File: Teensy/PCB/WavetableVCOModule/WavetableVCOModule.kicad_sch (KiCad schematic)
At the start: 11 parts, among them J1 Micro_SD_Card, SW1 Next_File_Button, U1 SPI_Oled, U2 Teensy4.0

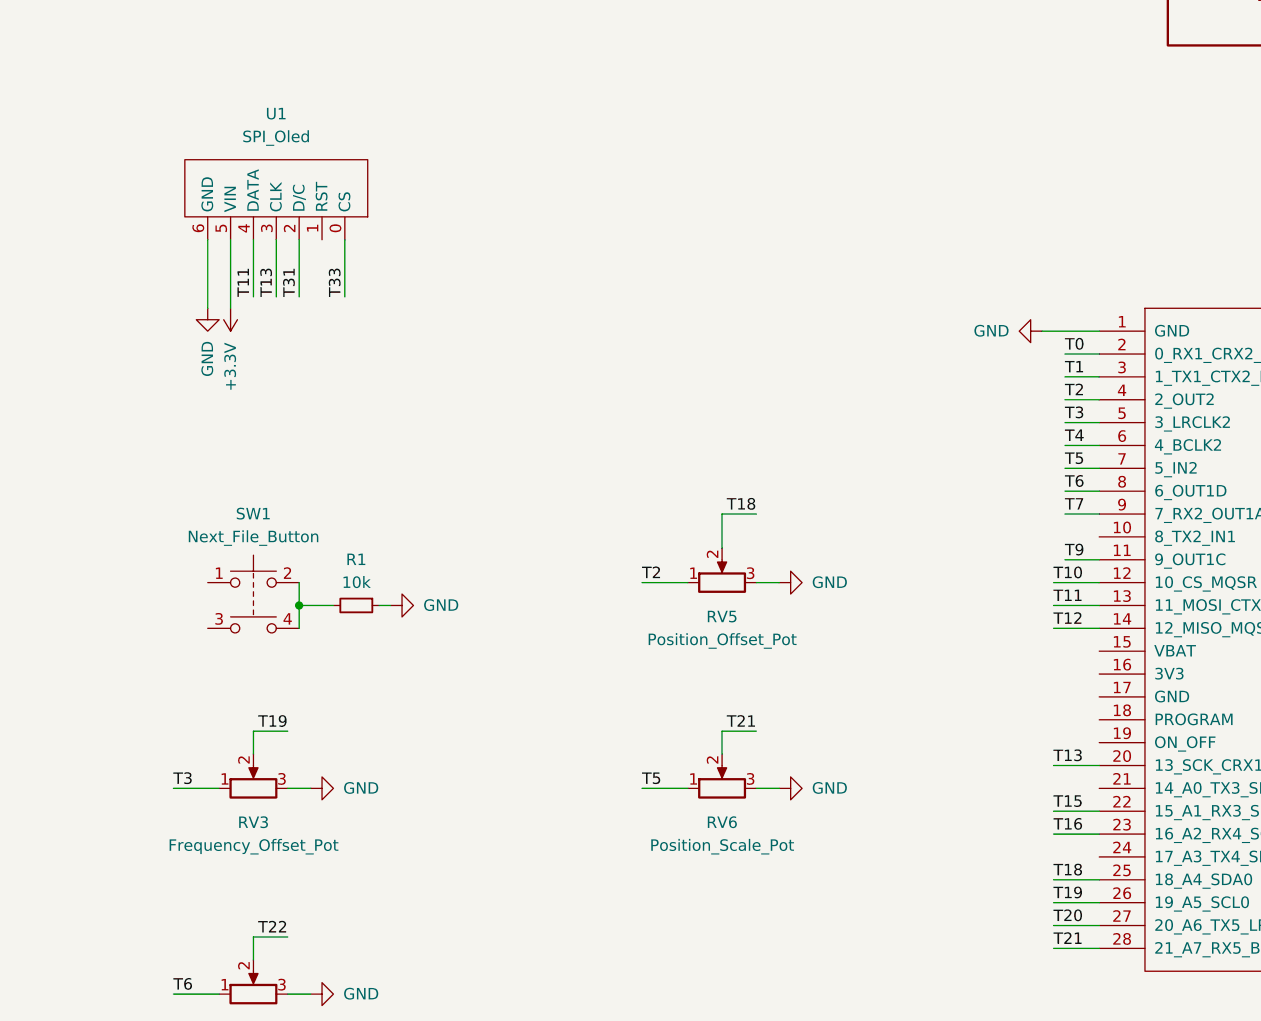
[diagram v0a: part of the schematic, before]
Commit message: Added Wavetable VCO
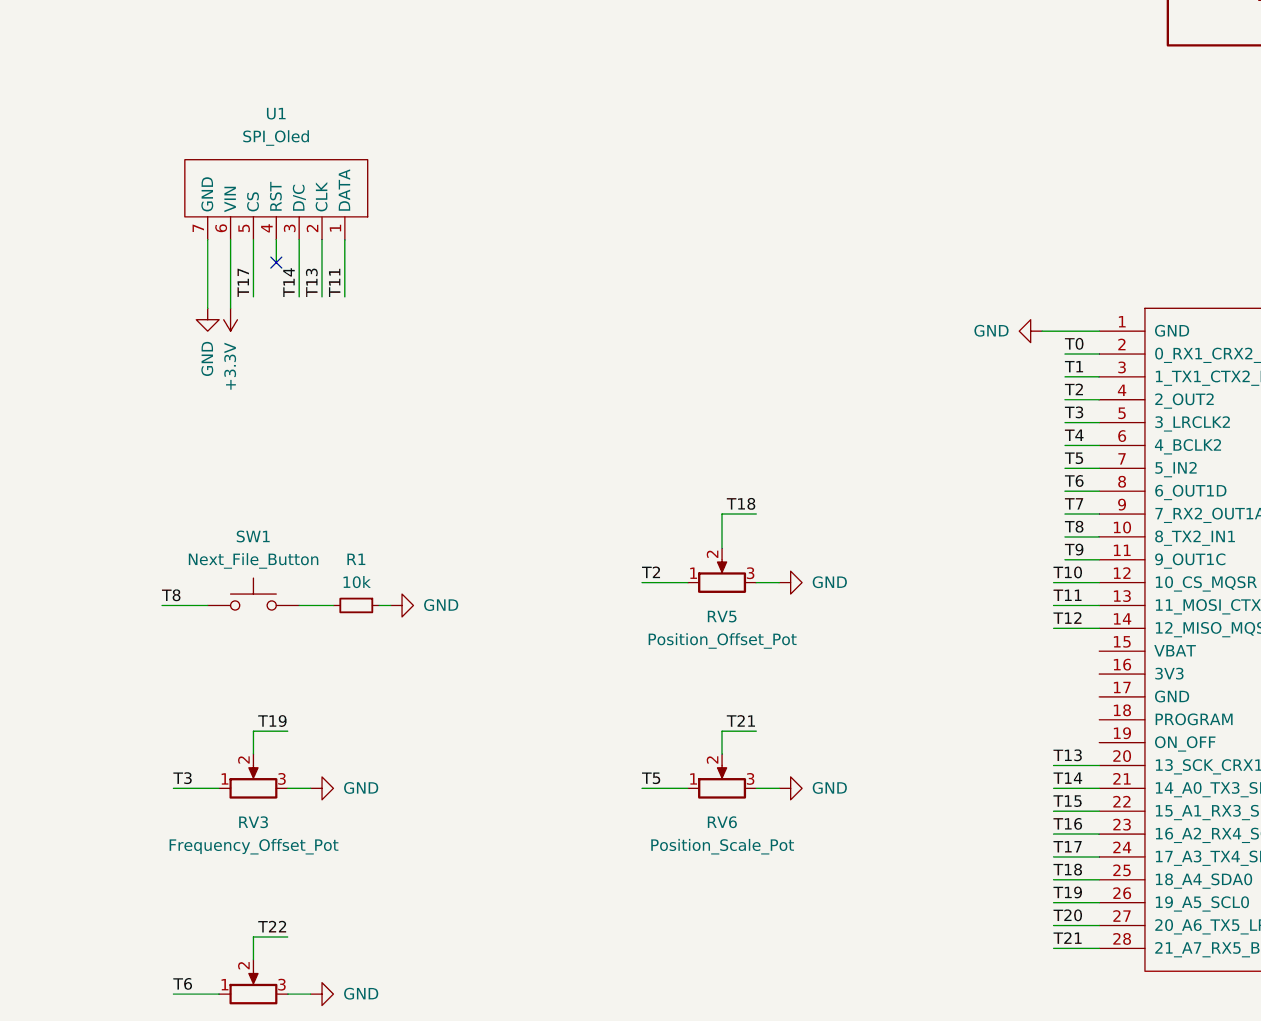
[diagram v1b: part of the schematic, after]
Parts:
- removed SW1: Next_File_Button, symbol Switch:SW_Push_Dual
- added SW1: Next_File_Button, symbol Switch:SW_Push
- J1: footprint (none) -> Misc:MSD4A
- R1: footprint (none) -> Resistor_SMD:R_1206_3216Metric_Pad1.30x1.75mm_HandSolder
- U1: footprint (none) -> Misc:1.5_inch_Oled
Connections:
- net T31 is gone; now on net T13: U1.2 (CLK)
- net +3.3V: now also U1.6 (VIN); no longer U1.5 (VIN)
- net GND: now also U1.7 (GND); no longer U1.6 (GND)
- net T11: now also U1.1 (DATA); no longer U1.4 (DATA)
- net T13: no longer U1.3 (CLK)
- net at R1.2: now also SW1.2
- net T8: now reaches U2.10 (8_TX2_IN1)
- net T8: now also SW1.1
- net T14: now reaches U2.21 (14_A0_TX3_SPDIF_OUT)
- net T14: now also U1.3 (D/C)
- net T17: now reaches U2.24 (17_A3_TX4_SDA1)
- net T17: now also U1.5 (CS)
- removed net T33: U1.0 (CS)
- no-connect marks 2 -> 3

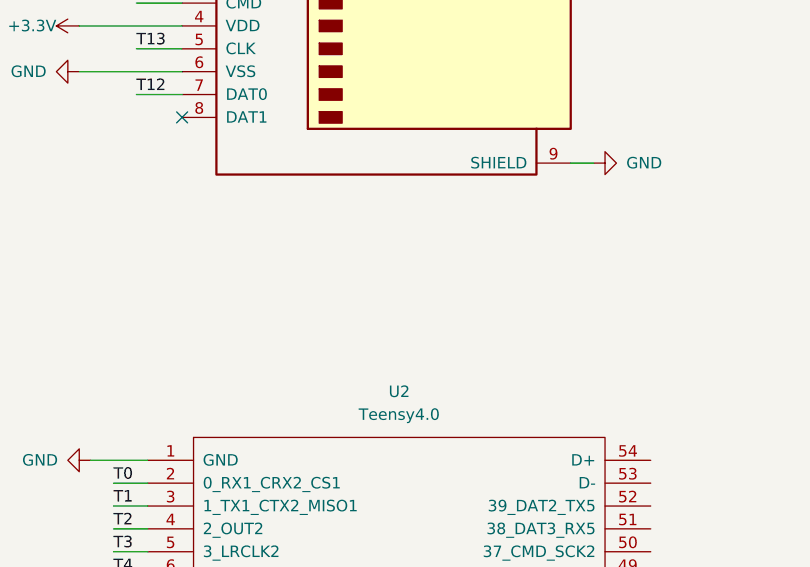
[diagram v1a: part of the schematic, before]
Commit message: Added Power connector and bracket
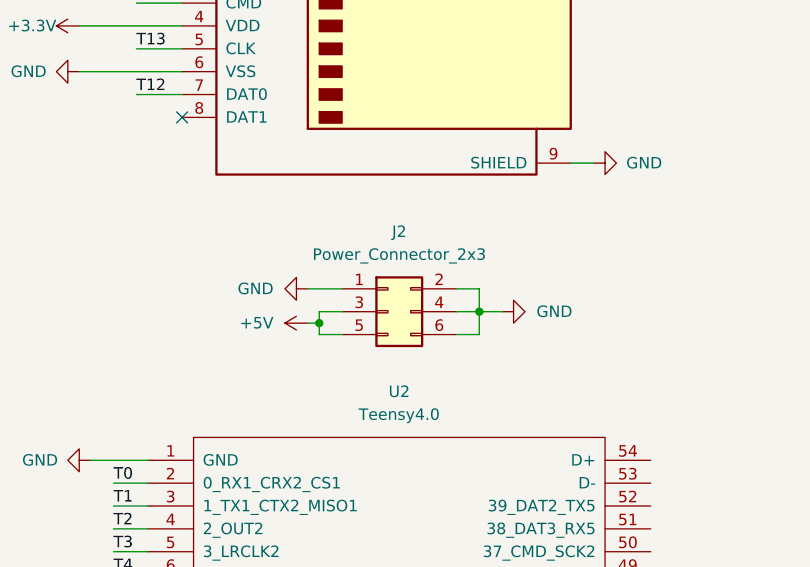
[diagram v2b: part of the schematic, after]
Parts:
- added J2: Power_Connector_2x3, Connector_PinHeader_2.54mm:PinHeader_2x03_P2.54mm_Vertical_SMD, symbol Connector_Generic:Conn_02x03_Odd_Even
- SW1: footprint (none) -> Button_Switch_THT:SW_PUSH_6mm_H13mm
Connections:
- net +5V: now also J2.3 (Pin_3), J2.5 (Pin_5)
- net GND: now also J2.1 (Pin_1), J2.2 (Pin_2), J2.4 (Pin_4), J2.6 (Pin_6)
